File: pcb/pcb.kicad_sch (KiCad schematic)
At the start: 8 parts, among them U1 ICM7555xP

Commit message: fix some errors
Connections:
- net 3Volt: no longer ON1.2, R3.2, U1.2 (TR)
- new net: ON1.2, R3.2, U1.2 (TR)
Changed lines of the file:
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@@
-	)
-	(junction
-		(at 177.8 86.36)
-		(diameter 0)
-		(color 0 0 0 0)
 	)
 	(junction
@@
 	(junction
 		(at 187.96 77.47)
-		(diameter 0)
-		(color 0 0 0 0)
-	)
-	(junction
-		(at 187.96 78.74)
 		(diameter 0)
 		(color 0 0 0 0)
@@
 	(wire
 		(pts
-			(xy 187.96 78.74) (xy 187.96 81.28)
+			(xy 187.96 77.47) (xy 187.96 81.28)
 		)
 		(stroke
@@
 	(wire
 		(pts
-			(xy 187.96 78.74) (xy 177.8 78.74)
-		)
-		(stroke
-			(width 0)
-			(type default)
-		)
-	)
-	(wire
-		(pts
 			(xy 166.37 105.41) (xy 175.26 105.41)
-		)
-		(stroke
-			(width 0)
-			(type default)
-		)
-	)
-	(wire
-		(pts
-			(xy 177.8 78.74) (xy 177.8 86.36)
 		)
 		(stroke
@@
 		)
 		(stroke
-			(width 0)
-			(type default)
-		)
-	)
-	(wire
-		(pts
-			(xy 187.96 77.47) (xy 187.96 78.74)
-		)
-		(stroke

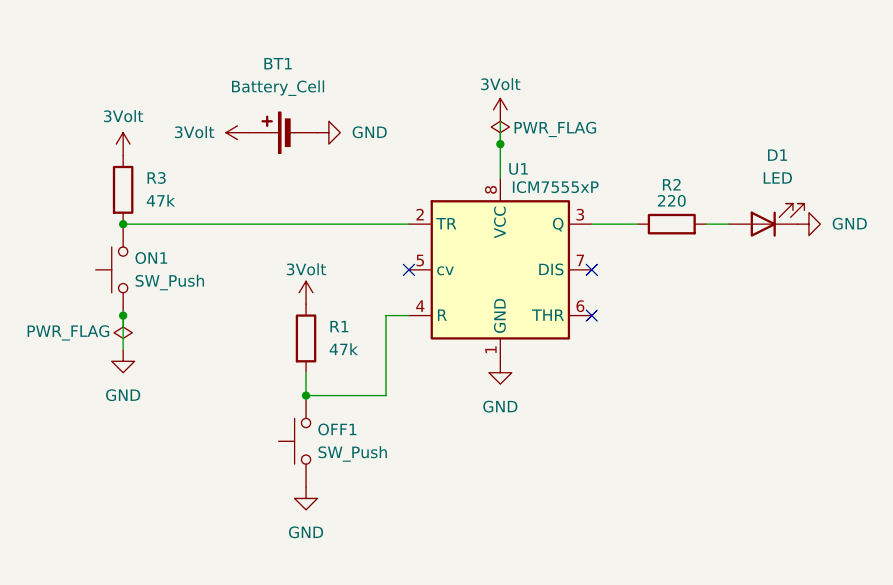
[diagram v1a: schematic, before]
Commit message: add some components
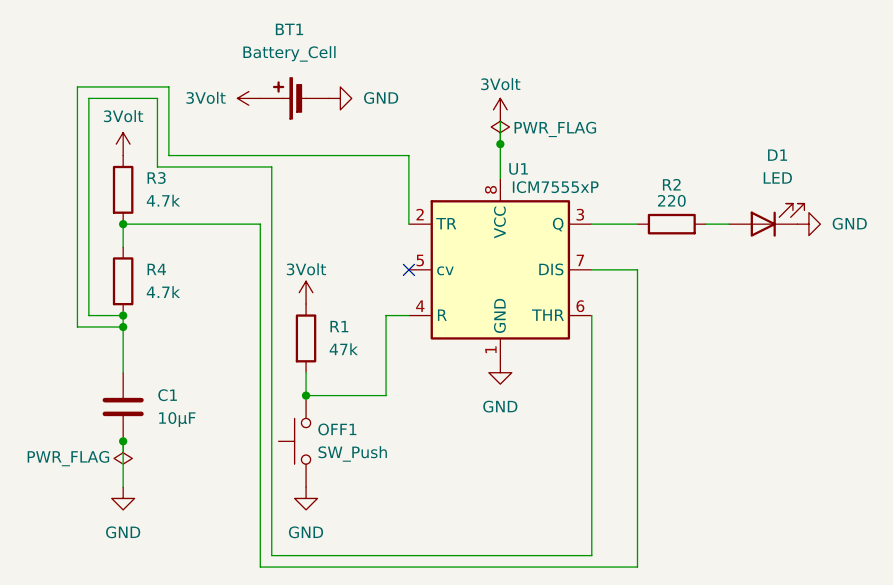
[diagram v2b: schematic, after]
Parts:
- removed ON1: SW_Push, Button_Switch_THT:SW_PUSH_6mm, symbol Switch:SW_Push
- added C1: 10µF, Capacitor_THT:CP_Radial_D8.0mm_P5.00mm, symbol Device:C
- added R4: 4.7k, Resistor_THT:R_Axial_DIN0207_L6.3mm_D2.5mm_P7.62mm_Horizontal, symbol Device:R
- R3: value 47k -> 4.7k
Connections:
- net GND: now also C1.2
- net at U1.2 (TR): now also U1.6 (THR), C1.1, R4.2; no longer R3.2
- net at U1.7 (DIS): now also R3.2, R4.1
- no-connect marks 3 -> 1
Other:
- moved on the sheet: BT1
